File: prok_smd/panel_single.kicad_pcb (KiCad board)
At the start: 2 copper layers, 20 x 128.5 mm, 2 parts

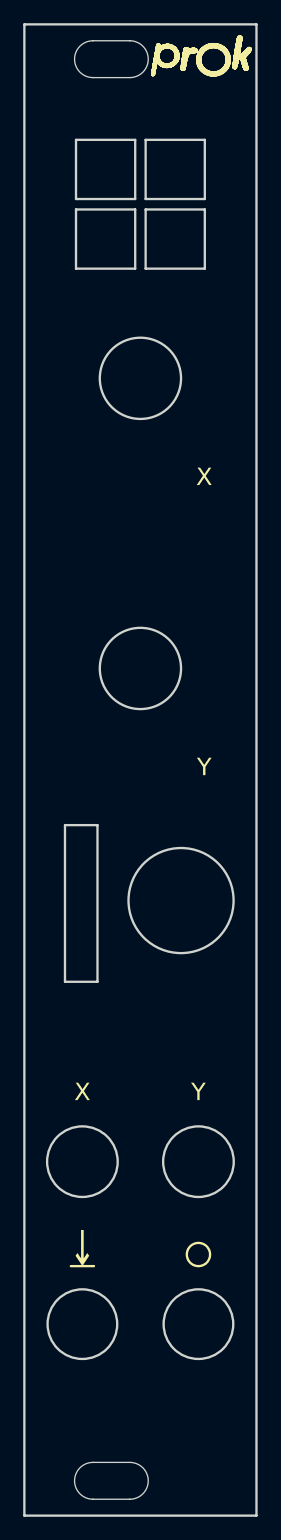
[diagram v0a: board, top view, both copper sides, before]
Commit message: :lipstick: :sparkles: Gold (soldermask hole) instead of silkscreen
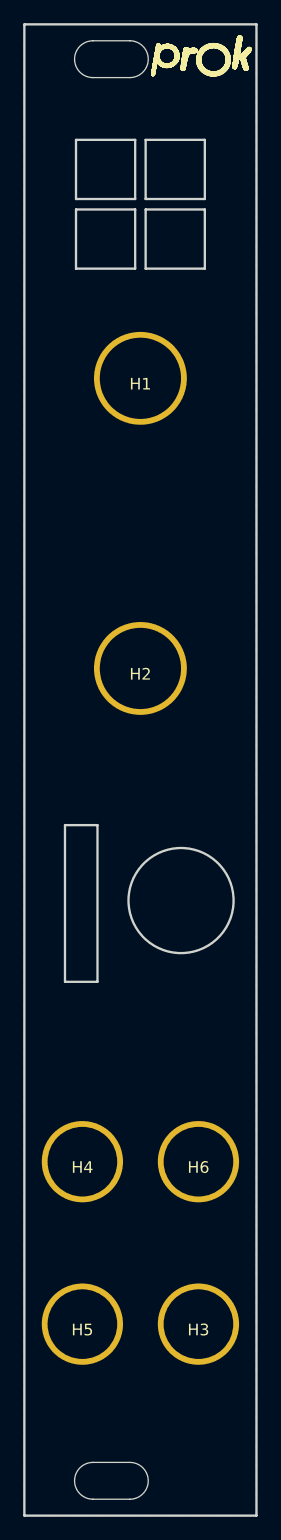
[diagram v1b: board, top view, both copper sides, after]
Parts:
- added H1: MountingHole_Pad, prok_smd:Alpha_pot_hole_metallized, F.Cu at (50.0, 60.5)
- added H2: MountingHole_Pad, prok_smd:Alpha_pot_hole_metallized, F.Cu at (50.0, 85.5)
- added H3: MountingHole_Pad, prok_smd:thonkiconn_hole_metallized, F.Cu at (55.0, 142.0)
- added H4: MountingHole_Pad, prok_smd:thonkiconn_hole_metallized, F.Cu at (45.0, 128.0)
- added H5: MountingHole_Pad, prok_smd:thonkiconn_hole_metallized, F.Cu at (45.0, 142.0)
- added H6: MountingHole_Pad, prok_smd:thonkiconn_hole_metallized, F.Cu at (55.0, 128.0)
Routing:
- added copper zone on B.Cu, net GND
- added copper zone on F.Cu, net GND
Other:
- outline, holes or cut-outs redrawn
